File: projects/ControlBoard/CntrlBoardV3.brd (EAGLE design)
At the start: 73.7 x 76.2 mm, 120 parts, among them J1 HARWIN_06, J2 HARWIN_06, J3 HARWIN_06, J4 M80-54010, J5 HARWIN_06, J6 M80-54020, J7 M83-LMT1M2N36, J8 M80-5101005, J9 M50-3600542, M1 AON7522E, M2 SI4427BDY-T1-E3CT-ND, U1 MR25H40MDF, U10 LT6015, U11 LT6016, U12 TPS63001, U13 TPS63002, U14 MPU9250, U15 HMC5883L, U2 M24M02-DR, U3 SN74LVC1G125, U4 SN74LVC1G125, U6 MR25H40MDF, U7 AD7991-1, U8 LTC1380-GN, U9 LTC1380-GN

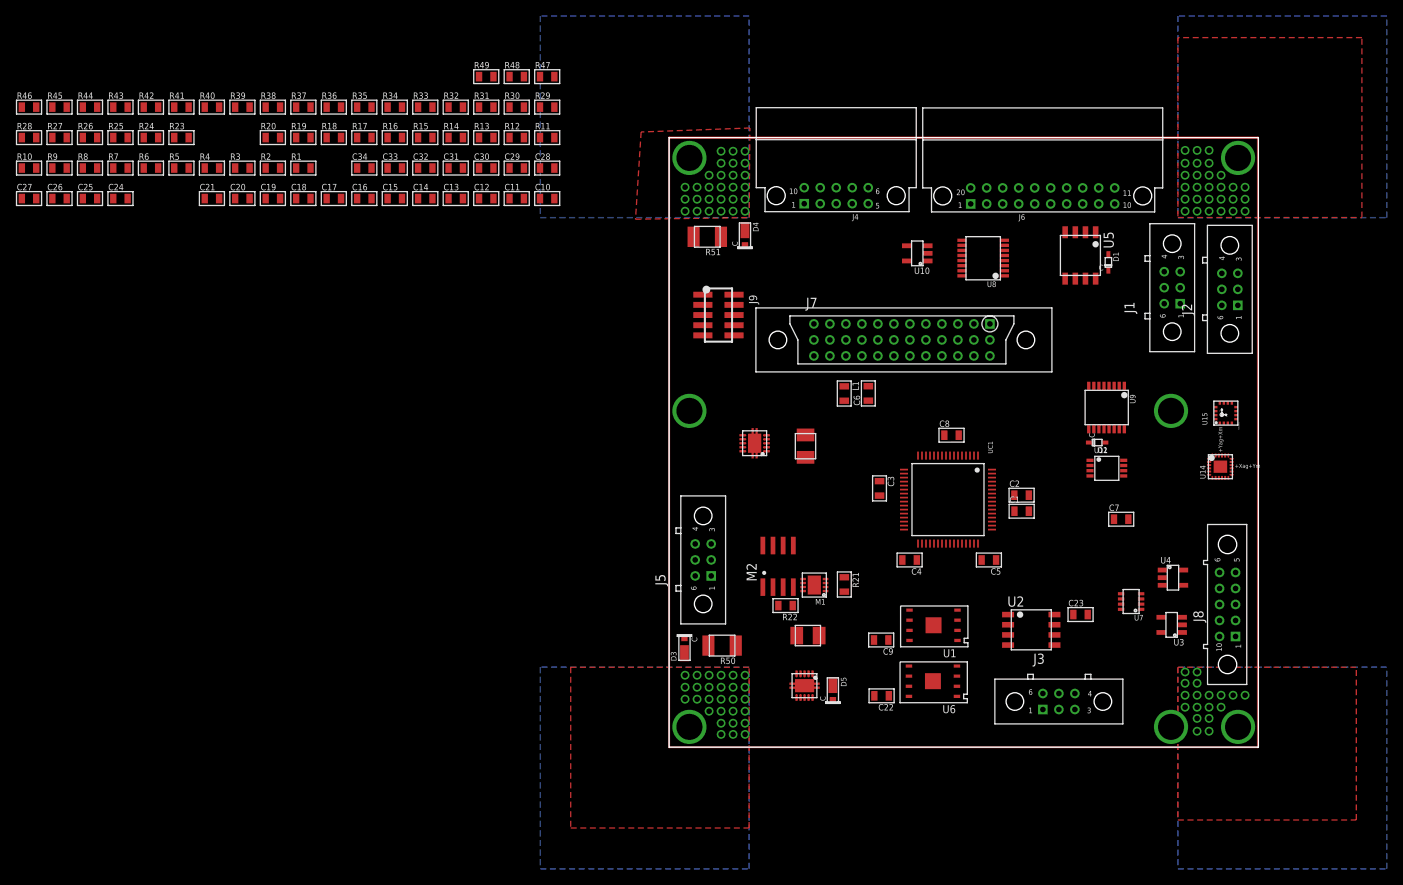
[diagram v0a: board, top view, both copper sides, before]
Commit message: Completed first round of cntrl board placement for all components.
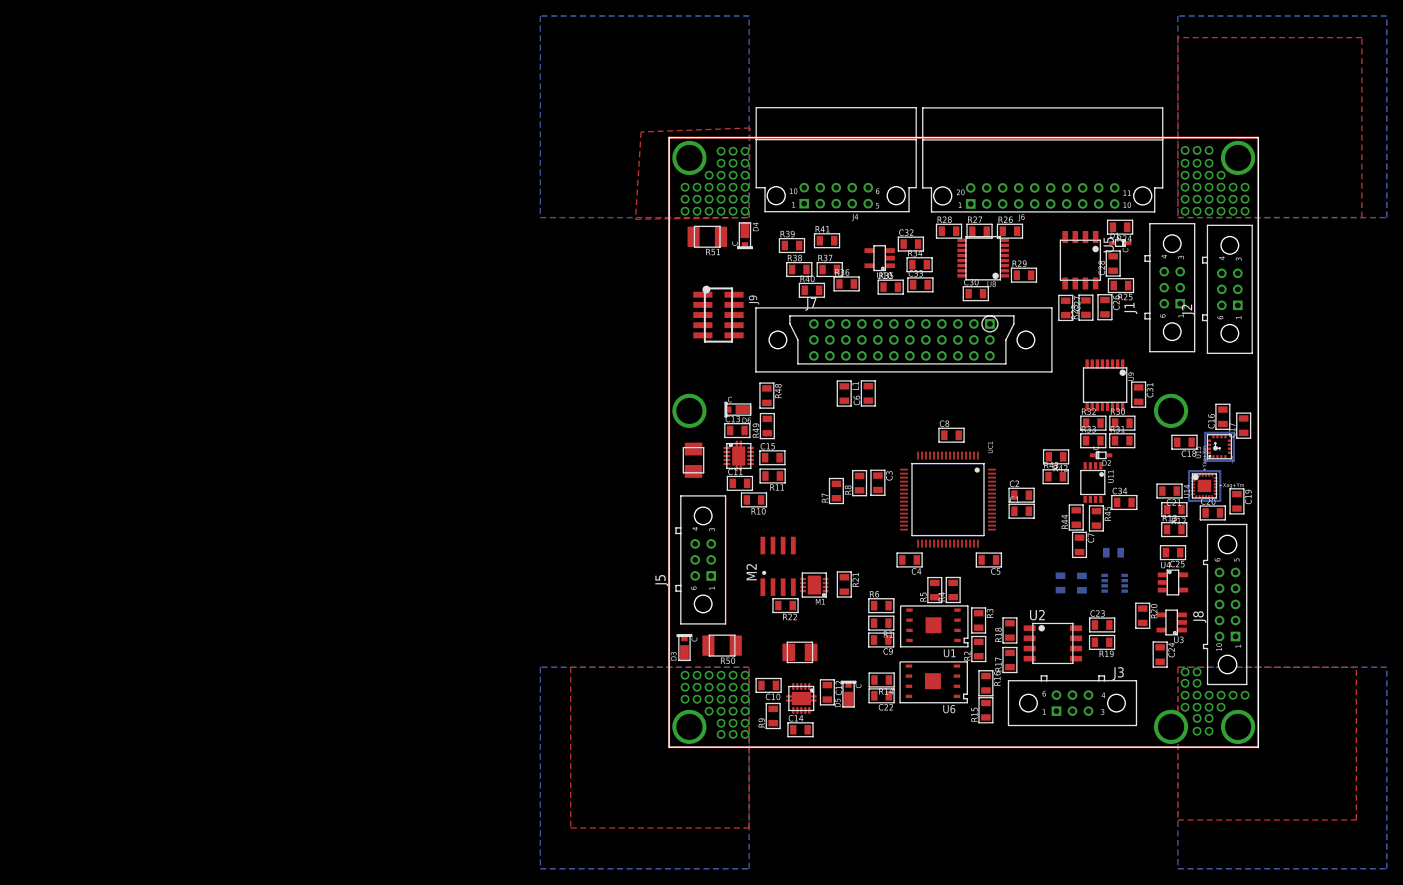
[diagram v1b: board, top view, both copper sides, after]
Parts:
- added D6: MSP5.0A, BrownSpaceEngineering:MICROSMP
- moved R46 144.4 mm to (51.6, 20.5), flipped to the bottom, turned to 270 degrees
- moved C25 142.4 mm to (63.0, 24.3), turned to 180 degrees
- moved C24 141.9 mm to (61.4, 11.6), turned to 270 degrees
- moved R45 139.4 mm to (53.4, 28.6), turned to 270 degrees
- moved R44 133.5 mm to (50.9, 28.7), turned to 90 degrees
- moved C26 131.4 mm to (54.5, 55.0), turned to 270 degrees
- moved C27 130.3 mm to (49.6, 54.9), turned to 270 degrees
- moved C20 127.5 mm to (68.0, 29.3)
- moved R25 126.4 mm to (56.5, 57.7), turned to 180 degrees
- moved C19 126.3 mm to (71.0, 30.7), turned to 270 degrees
- moved R43 125.7 mm to (48.3, 33.8)
- moved C21 125.2 mm to (62.5, 32.0), turned to 180 degrees
- moved R20 124.1 mm to (59.2, 16.4), turned to 270 degrees
- moved R24 121.7 mm to (56.4, 65.0), turned to 180 degrees
- moved R42 121.3 mm to (48.4, 36.3), turned to 180 degrees
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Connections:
- net +5V: now also D6.C
- net GND: now also D6.A
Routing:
- net N$37: track 0.00 -> 15.2 mm
- net N$36: track 0.00 -> 15.2 mm
- net N$35: track 0.00 -> 15.2 mm
- net N$32: track 0.00 -> 15.2 mm
- net N$31: track 0.00 -> 15.2 mm
- net N$39: track 0.00 -> 14.2 mm
- net N$30: track 0.00 -> 14.2 mm
- net N$29: track 0.00 -> 14.2 mm
- net N$28: track 0.00 -> 14.2 mm
- net N$26: track 0.00 -> 14.2 mm

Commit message: Continued work on Control Board layout - modification of some connector types and connector pinouts to optimize routing, initial power and ground routing.
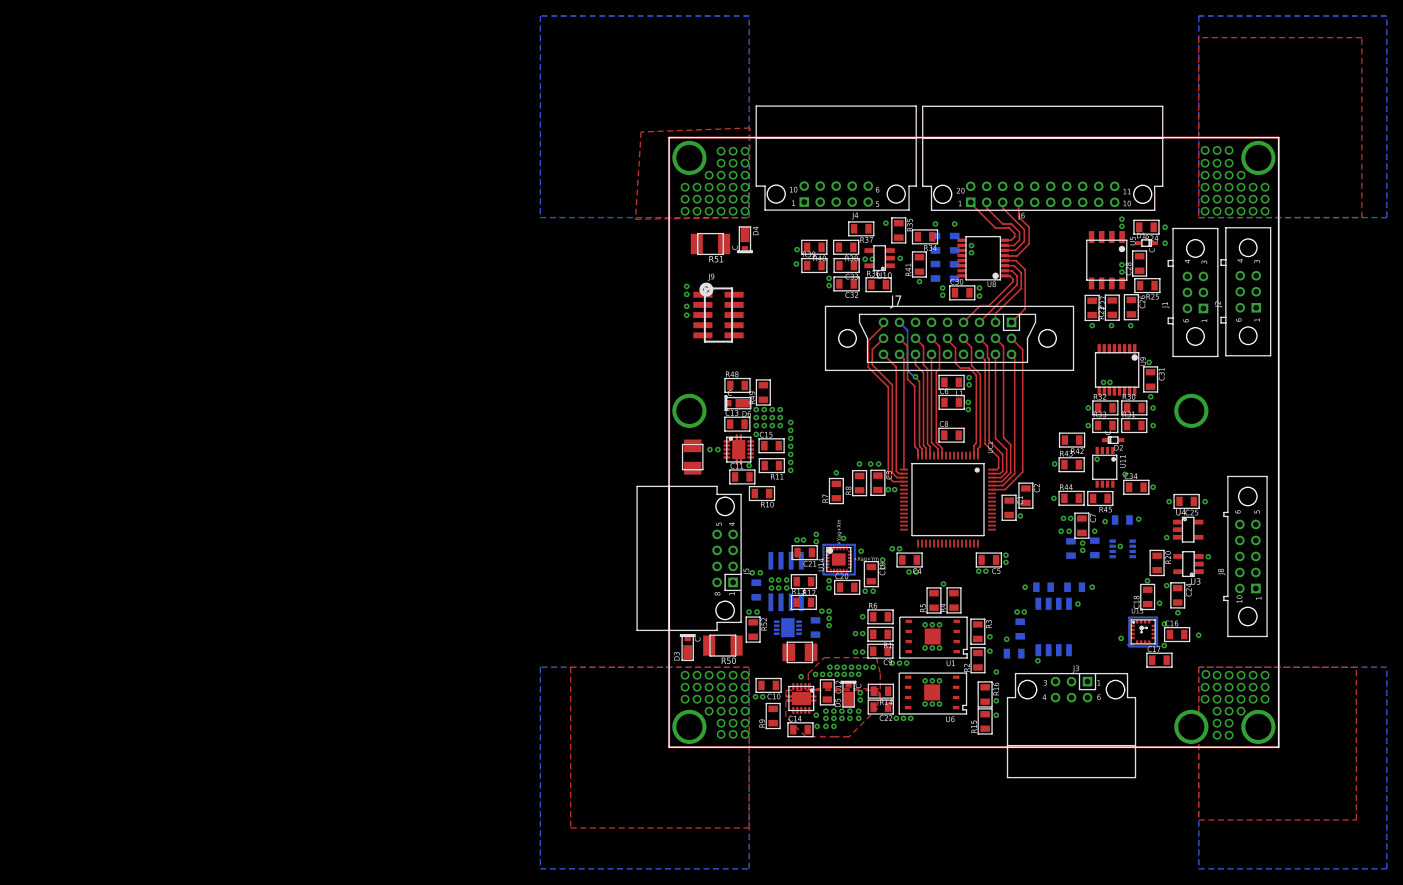
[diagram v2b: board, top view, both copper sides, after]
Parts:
- added R52: 10M, BrownSpaceEngineering:0805
- J3: value HARWIN_06 -> M80-54006; device CNTRL_BOARD:HARWIN_DATAMATE_6 -> BrownSpaceEngineering:M80-54006
- J5: value HARWIN_06 -> M80-54008; device CNTRL_BOARD:HARWIN_DATAMATE_6 -> BrownSpaceEngineering:M80-54008
- J7: value M83-LMT1M2N36 -> M83-LMT1M2N27; device BrownSpaceEngineering:M83-LMT1M2N36 -> BrownSpaceEngineering:M83-LMT1M2N27
- moved R13 47.2 mm to (16.8, 18.1)
- moved R12 47.2 mm to (16.9, 20.7)
- moved C20 46.6 mm to (22.3, 20.0)
- moved U14 46.6 mm to (21.2, 23.5)
- moved C19 46.6 mm to (25.3, 21.6)
- moved C21 46.2 mm to (16.9, 24.3)
- moved C17 31.1 mm to (61.3, 10.9), turned to 0 degrees
- moved C16 27.8 mm to (63.5, 14.1), turned to 0 degrees
- moved U15 26.3 mm to (57.8, 12.9), turned to 0 degrees
- moved C18 19.9 mm to (59.8, 18.8), turned to 90 degrees
- moved L1 13.5 mm to (35.3, 45.6), turned to 180 degrees
- moved R17 12.2 mm to (50.7, 20.0), flipped to the bottom, turned to 0 degrees
- moved R41 11.9 mm to (31.3, 60.3), turned to 90 degrees
- moved R19 11.1 mm to (43.1, 11.7), flipped to the bottom
- moved C6 10.5 mm to (35.3, 43.1), turned to 0 degrees
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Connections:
- removed net !BATT_INT!: UC1.P$13
- removed net L1_CHGN: J7.P$30
- removed net L1_FAULTN: J7.P$29
- removed net L2_CHGN: J7.P$32
- removed net L2_FAULTN: J7.P$31
- removed net LION1REF: UC1.P$3
- removed net LION1_DISG: UC1.P$59
- removed net LION2REF: UC1.P$4
- removed net LION2_DISG: UC1.P$60
- removed net LION2_RUN_CHG: UC1.P$63
- removed net LION_OUT: J7.P$6
- net !CS2!: now also UC1.P$39; no longer UC1.P$44
- net !RAD_SHDN!: now also UC1.P$44; no longer UC1.P$40
- net +3V3: now also J7.P$6; no longer J7.P$10
- net +5V: now also J7.P$7; no longer J7.P$5
- net GND: now also J5.P$6, J7.P$5, R52.1; no longer J7.P$7
- net IR_PWR_CMD: now also UC1.P$40; no longer UC1.P$43
- net L1_DISG: now also J7.P$18, UC1.P$59; no longer J7.P$23
- net L1_REF: now also UC1.P$16
- net L1_RUN_CHG: now also J7.P$17, UC1.P$61; no longer J7.P$21
- net L2_DISG: now also J7.P$19, UC1.P$60; no longer J7.P$24
- net L2_REF: now also J7.P$8, UC1.P$15; no longer J7.P$12
- net L2_RUN_CHG: now also J7.P$16, UC1.P$63; no longer J7.P$22
- net LF1REF: now also J7.P$25, UC1.P$14; no longer J7.P$15, UC1.P$5
- net LF2REF: now also J7.P$12, UC1.P$13; no longer J7.P$16, UC1.P$6
- net LF3REF: now also J7.P$13, UC1.P$10; no longer J7.P$19, UC1.P$9
- net LF4REF: now also J7.P$24, UC1.P$11; no longer J7.P$20, UC1.P$10
- net LFB1OSNS: now also J7.P$9; no longer J7.P$13
- net LFB1SNS: now also J7.P$10; no longer J7.P$14
- net LFB2OSNS: now also J7.P$27; no longer J7.P$17
- net LFB2SNS: now also J7.P$26; no longer J7.P$18
- net LF_B1_OUTEN: now also J7.P$15; no longer J7.P$26
- net LF_B1_RUNCHG: now also J7.P$21; no longer J7.P$25
- net LF_B2_OUTEN: now also J7.P$14; no longer J7.P$28
- net LF_B2_RUNCHG: now also J7.P$20; no longer J7.P$27, UC1.P$61
- net PD_OUT: now also UC1.P$3; no longer UC1.P$16
- net RAD_PWR_RUN: now also UC1.P$43; no longer UC1.P$39
- net SCL: now also J3.P$3, J7.P$23; no longer J3.P$2, J7.P$9
- net SDA: now also J3.P$2, J7.P$22; no longer J3.P$3, J7.P$8
- net TEMP_OUT: now also UC1.P$4; no longer UC1.P$15
- net VIN: now also R52.2
- net VIN-INT: now also J5.P$7, J5.P$8; no longer J5.P$6
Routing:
- net LFB1OSNS: track 0.00 -> 23.3 mm
- net L1_DISG: track 0.00 -> 22.0 mm
- net L1_RUN_CHG: track 0.00 -> 20.4 mm
- net LFB1SNS: track 0.00 -> 20.1 mm
- net L2_RUN_CHG: track 0.00 -> 19.3 mm
- net L2_DISG: track 0.00 -> 18.5 mm
- net L2_REF: track 0.00 -> 17.9 mm, vias 0 -> 1
- net LF_B2_RUNCHG: track 0.00 -> 17.4 mm
- net LF_B2_OUTEN: track 0.00 -> 16.9 mm
- net LFB2OSNS: track 0.00 -> 16.3 mm
- net LF_B1_RUNCHG: track 0.00 -> 16.1 mm
- net LF_B1_OUTEN: track 0.00 -> 15.6 mm
- net L1_REF: track 0.00 -> 15.6 mm
- net LF3REF: track 0.00 -> 15.5 mm
- net LF2REF: track 0.00 -> 15.4 mm
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- added copper zone on layer 1, net +3V3
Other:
- board size 73.7 x 76.2 mm -> 76.2 x 76.2 mm

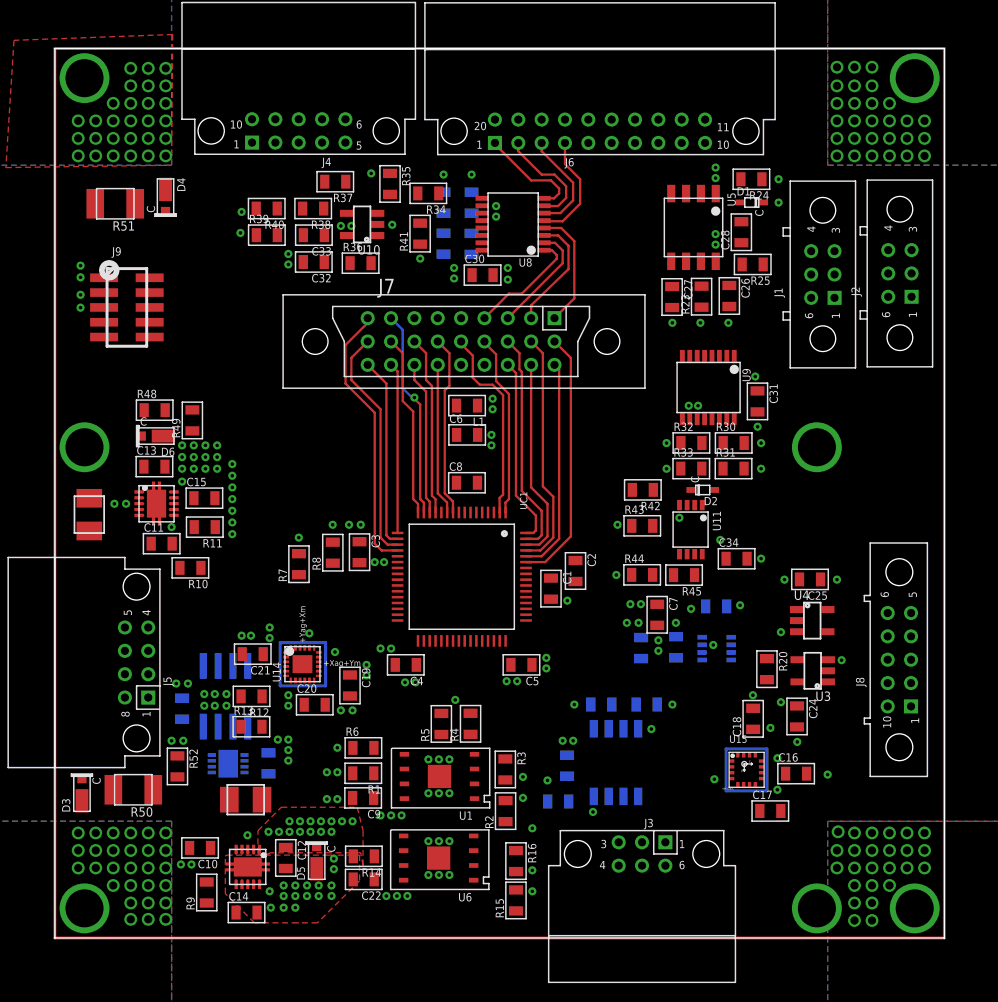
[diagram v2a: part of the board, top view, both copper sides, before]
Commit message: Continued routing of Control Board.
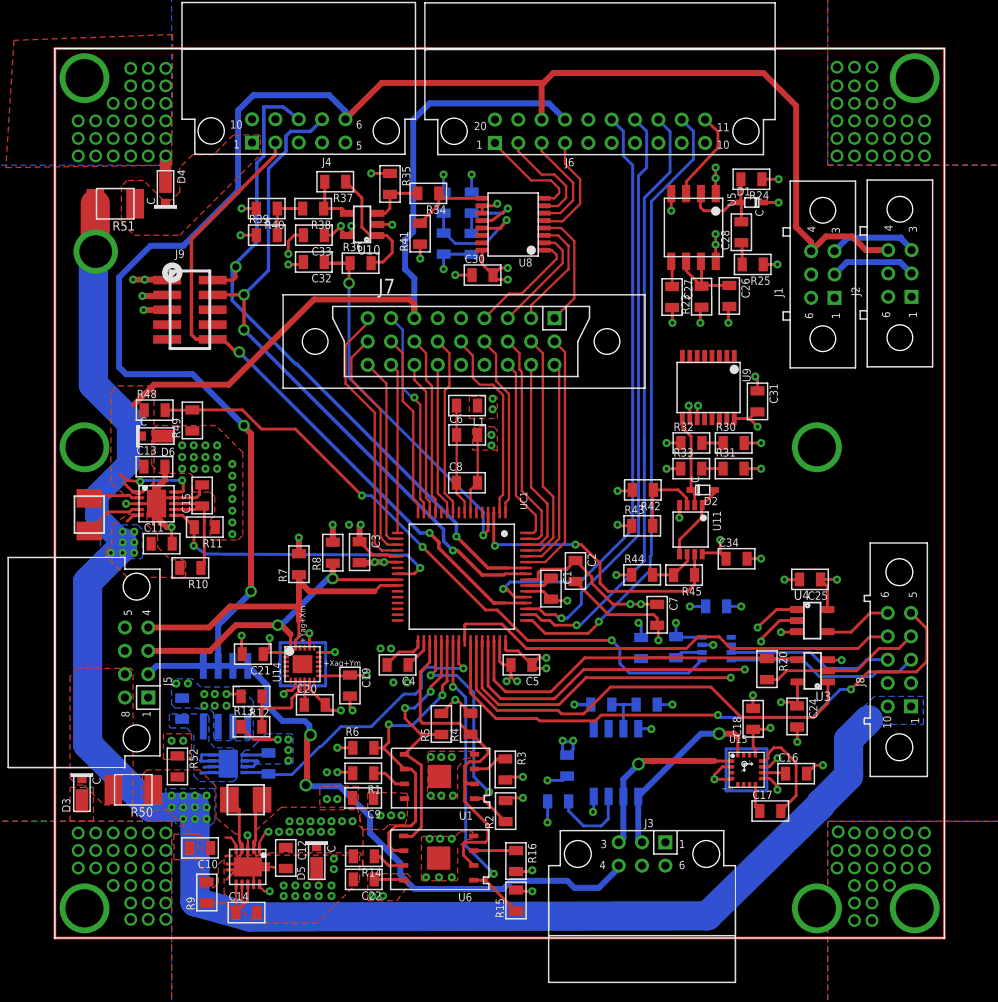
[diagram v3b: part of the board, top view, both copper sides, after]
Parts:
- moved J9 5.40 mm to (11.6, 53.8)
- moved D4 0.70 mm to (9.48, 63.5)
- moved C4 0.70 mm to (29.4, 23.4)
- moved C15 0.30 mm to (12.6, 37.9), turned to 90 degrees
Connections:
- net !RAD_SHDN!: now also UC1.P$42; no longer UC1.P$44
- net !RESET!: now also J4.P$2; no longer J4.P$6
- net ANT_DRV2: now also J6.P$8; no longer J6.P$10
- net ANT_DRV3: now also J6.P$7; no longer J6.P$11
- net DET_RTN: now also J6.P$6; no longer J6.P$7
- net GND: now also J6.P$5; no longer J6.P$6
- net IRVDD: now also J4.P$6, J5.P$2; no longer J4.P$4, J5.P$4
- net LED1SNS: now also J6.P$15; no longer J6.P$12
- net LED2SNS: now also J6.P$14; no longer J6.P$13
- net LED3SNS: now also J6.P$13; no longer J6.P$14
- net LED4SNS: now also J6.P$12; no longer J6.P$15
- net LED_SHDN: now also J6.P$11; no longer J6.P$5
- net PD_FLASH: now also J6.P$10; no longer J6.P$8
- net RAD_PWR_RUN: now also UC1.P$41; no longer UC1.P$43
- net RX_EN: now also UC1.P$43; no longer UC1.P$42
- net SCL: now also J4.P$4, J5.P$4; no longer J4.P$2, J5.P$2
- net TX_EN: now also UC1.P$44; no longer UC1.P$41
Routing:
- net IRVDD: track 0.00 -> 194.7 mm, vias 0 -> 4
- net VIN: track 0.00 -> 139.7 mm, vias 0 -> 19
- net GND: track 0.00 -> 139.6 mm, vias 237 -> 226
- net +3V3: track 0.00 -> 119.8 mm, vias 81 -> 80
- net +5V: track 0.00 -> 69.5 mm, vias 0 -> 2
- net SWDIO: track 0.00 -> 59.3 mm, vias 0 -> 2
- net SWDCLK: track 0.00 -> 58.2 mm, vias 0 -> 3
- net !RESET!: track 0.00 -> 57.9 mm, vias 0 -> 2
- net 5VREF: track 0.00 -> 56.6 mm, vias 0 -> 3
- net LED4SNS: track 0.00 -> 53.9 mm, vias 0 -> 1
- net LED3SNS: track 0.00 -> 53.8 mm, vias 0 -> 1
- net SCL: track 0.00 -> 52.0 mm, vias 0 -> 1
- net SDA: track 0.00 -> 51.9 mm, vias 0 -> 3
- net !RAD_SHDN!: track 0.00 -> 51.5 mm, vias 0 -> 2
- net LED1SNS: track 0.00 -> 51.4 mm, vias 0 -> 1
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- added copper zone on layer 16, net +3V3
- added copper zone on layer 1, net +5V
- added copper zone on layer 16, net N$22
- added copper zone on layer 1, net VIN
- added copper zone on layer 16, net VIN
- added copper zone on layer 1, net VIN-EXT
- added copper zone on layer 1, net VIN-INT
